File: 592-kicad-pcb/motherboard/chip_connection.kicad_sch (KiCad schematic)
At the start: 12 parts, among them J4 Conn_02x16_Odd_Even, J5 Conn_01x16

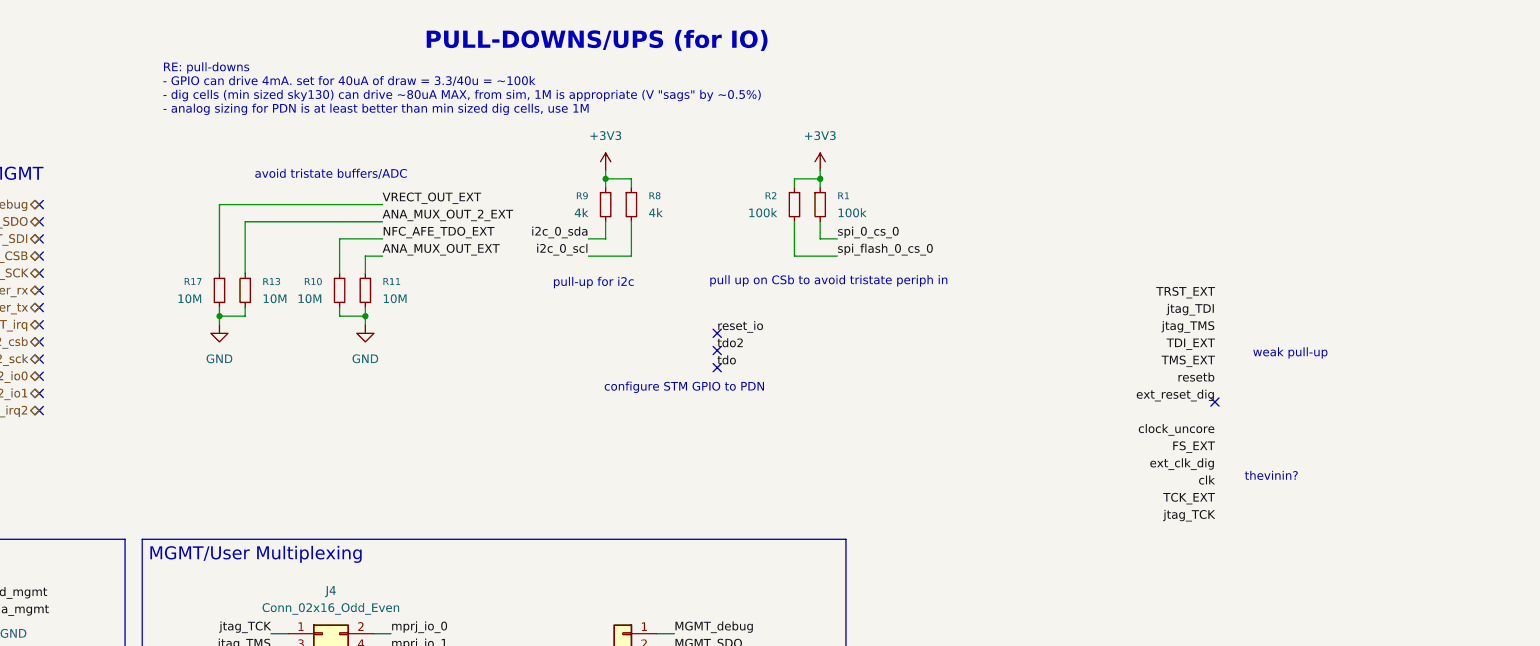
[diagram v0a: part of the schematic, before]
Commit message: update ftdi chip
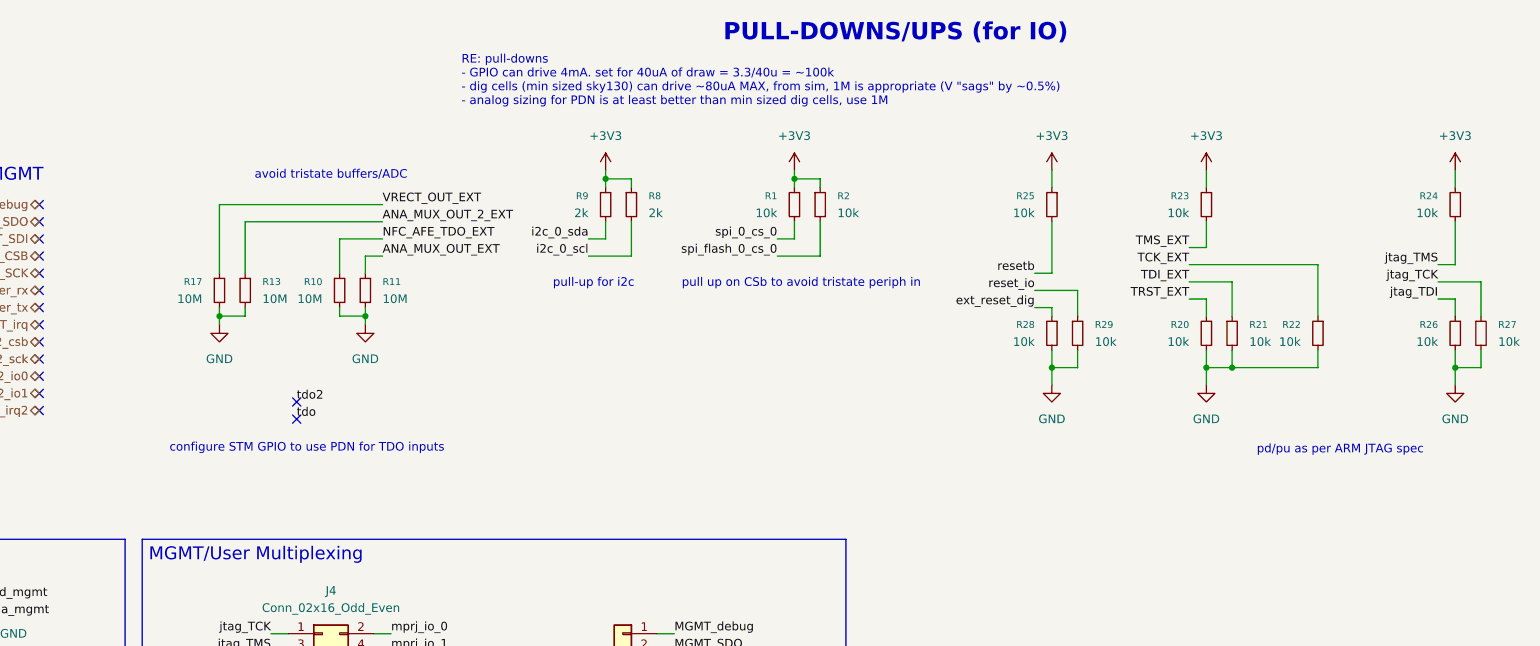
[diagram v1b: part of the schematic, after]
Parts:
- added R20, R21, R22, R23, R24, R25, R26, R27, R28, R29: 10k, symbol Device:R_Small
- R1, R2: value 100k -> 10k
- R8, R9: value 4k -> 2k
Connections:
- net +3V3: now also R23.1, R24.1, R25.1
- net GND: now also R20.2, R21.2, R22.2, R26.2, R27.2, R28.2, R29.2
- net TCK_EXT: now also R22.1
- net TDI_EXT: now also R21.1
- net TMS_EXT: now also R23.2
- net TRST_EXT: now also R20.1
- net ext_reset_dig: now also R28.1
- net jtag_TCK: now also R27.1
- net jtag_TDI: now also R26.1
- net jtag_TMS: now also R24.2
- net reset_io: now also R29.1
- net resetb: now also R25.2
- no-connect marks 65 -> 63
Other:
- note added: "configure STM GPIO to use PDN for TDO inputs"
- note added: "pd/pu as per ARM JTAG spec"
- note removed: "configure STM GPIO to PDN"
- note removed: "thevinin?"
- note removed: "weak pull-up"
- moved on the sheet: R1, R2

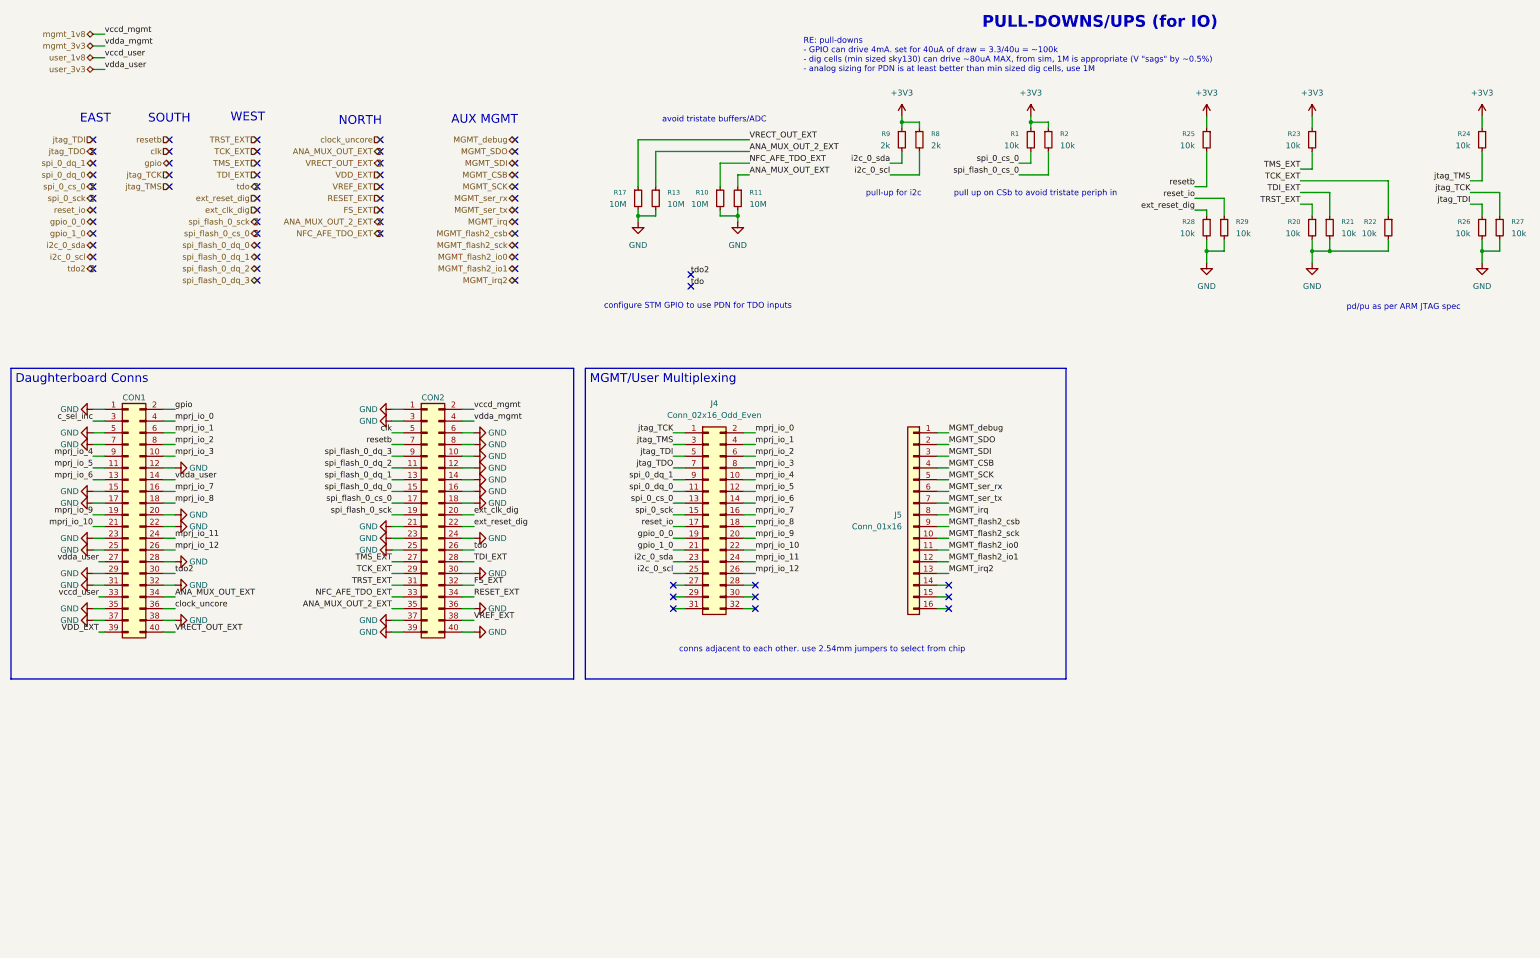
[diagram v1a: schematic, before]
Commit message: combine hierarchy of all sans power
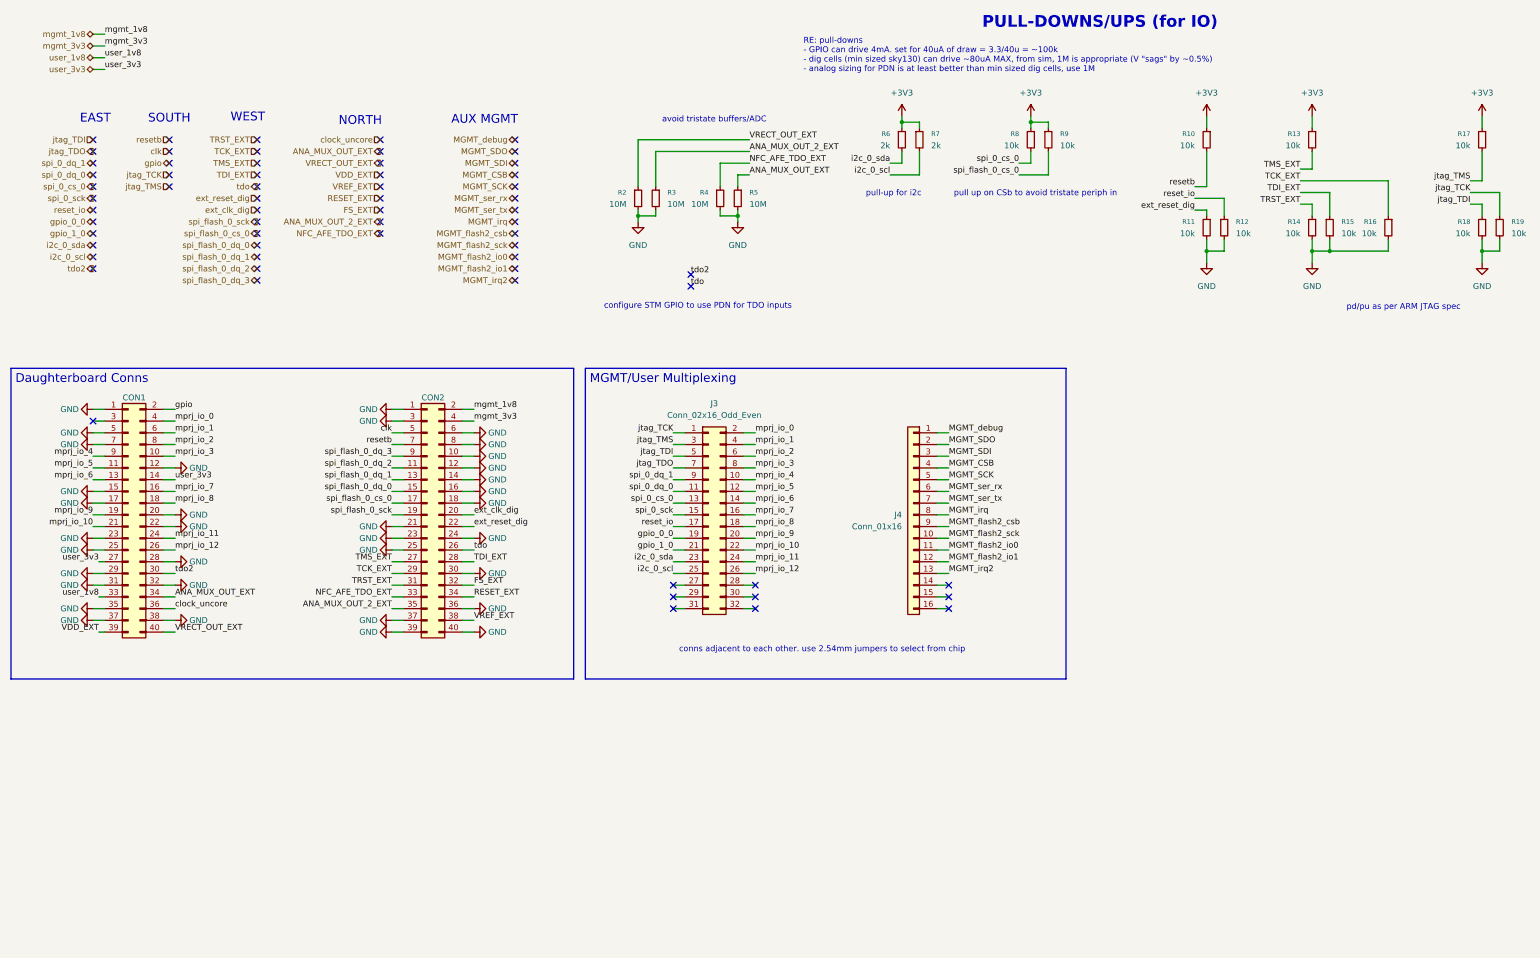
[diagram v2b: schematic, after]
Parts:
- renumbered J4 to J3, J5 to J4, R25 to R10, R28 to R11, R29 to R12, R23 to R13, R20 to R14, R21 to R15, R22 to R16, R24 to R17, R26 to R18, R27 to R19, R17 to R2, R13 to R3, R10 to R4, R11 to R5, R9 to R6, R8 to R7, R1 to R8, R2 to R9
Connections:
- net c_sel_inc: no longer names the net of CON1.3 (Pin_3)
- no-connect marks 63 -> 64

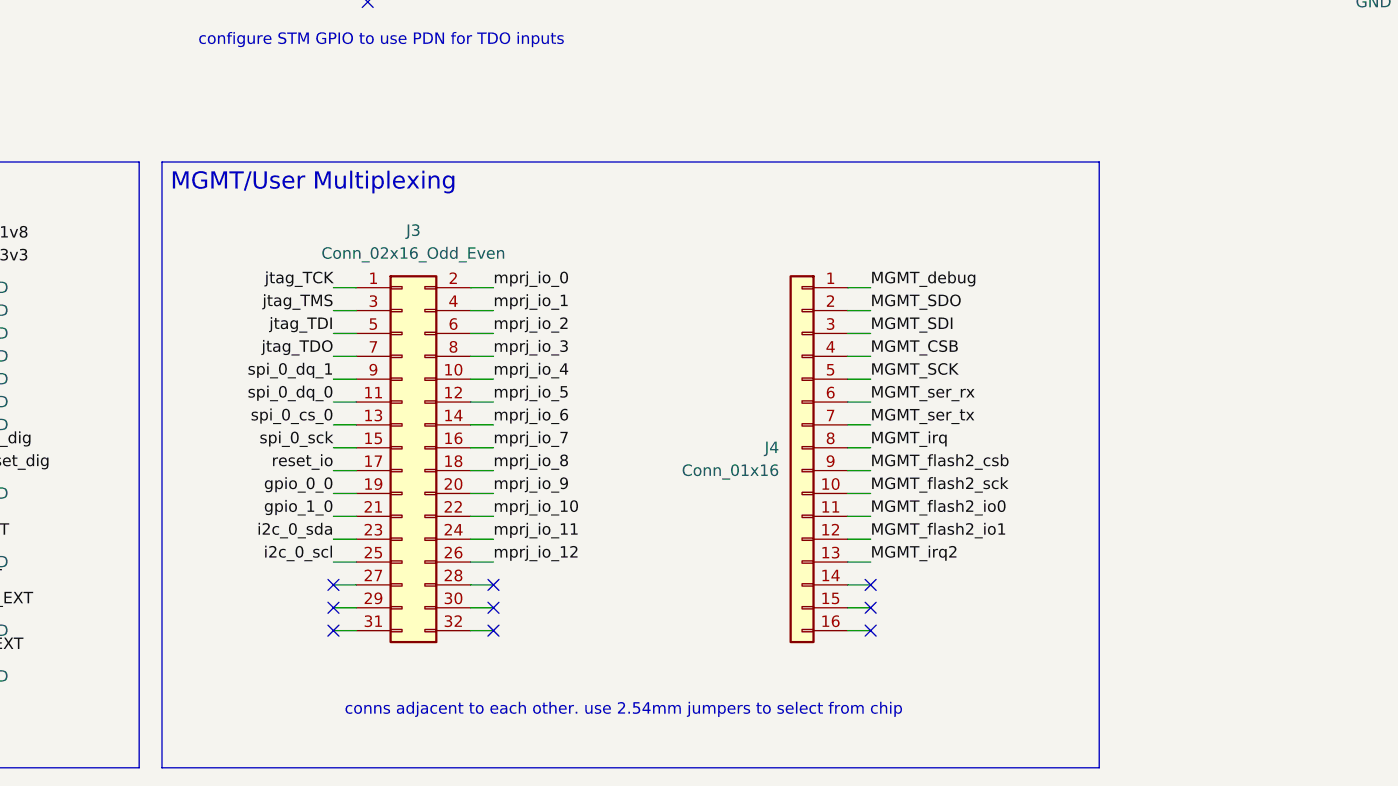
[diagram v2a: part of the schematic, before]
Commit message: add JLC part num for parts, footprints
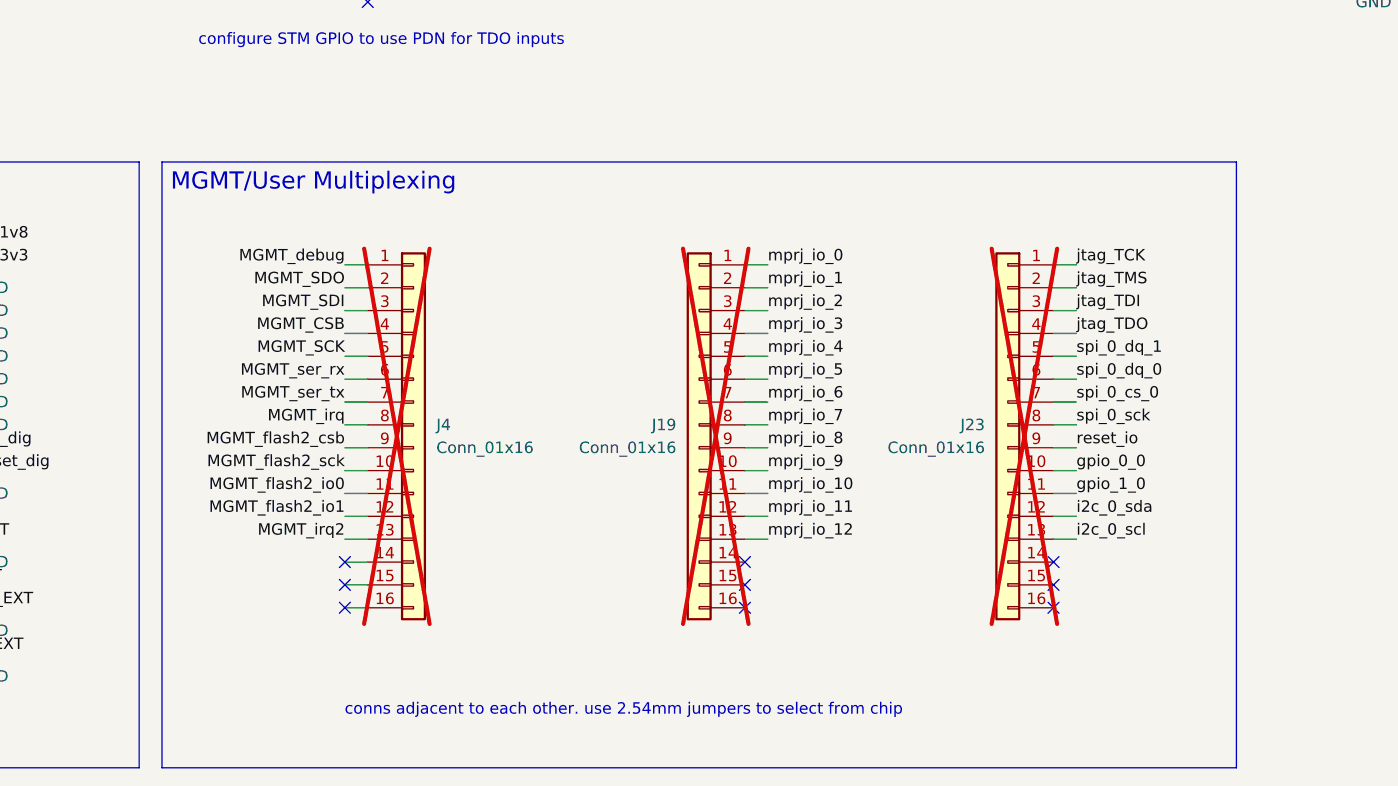
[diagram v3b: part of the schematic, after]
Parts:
- removed J3: Conn_02x16_Odd_Even, symbol Connector_Generic:Conn_02x16_Odd_Even
- added J19, J23: Conn_01x16, Connector_PinHeader_2.54mm:PinHeader_1x16_P2.54mm_Vertical, symbol Connector_Generic:Conn_01x16
- CON1, CON2: footprint TinyTapeout:FH-00148_PinSocket_2x20_P2.54mm -> (none)
- J4: footprint (none) -> Connector_PinHeader_2.54mm:PinHeader_1x16_P2.54mm_Vertical; now not fitted
- R10, R11, R12, R13, R14, R15, R16, R17, R18, R19, R8, R9: footprint (none) -> Resistor_SMD:R_0603_1608Metric; LCSC (none) -> C25804
- R2, R3, R4, R5: footprint (none) -> Resistor_SMD:R_0603_1608Metric; LCSC (none) -> C7250
- R6, R7: footprint (none) -> Resistor_SMD:R_0603_1608Metric; LCSC (none) -> C22975
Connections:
- net gpio_0_0: now also J23.10 (Pin_10)
- net gpio_1_0: now also J23.11 (Pin_11)
- net i2c_0_scl: now also J23.13 (Pin_13)
- net i2c_0_sda: now also J23.12 (Pin_12)
- net jtag_TCK: now also J23.1 (Pin_1)
- net jtag_TDI: now also J23.3 (Pin_3)
- net jtag_TDO: now also J23.4 (Pin_4)
- net jtag_TMS: now also J23.2 (Pin_2)
- net mprj_io_0: now also J19.1 (Pin_1)
- net mprj_io_1: now also J19.2 (Pin_2)
- net mprj_io_10: now also J19.11 (Pin_11)
- net mprj_io_11: now also J19.12 (Pin_12)
- net mprj_io_12: now also J19.13 (Pin_13)
- net mprj_io_2: now also J19.3 (Pin_3)
- net mprj_io_3: now also J19.4 (Pin_4)
- net mprj_io_4: now also J19.5 (Pin_5)
- net mprj_io_5: now also J19.6 (Pin_6)
- net mprj_io_6: now also J19.7 (Pin_7)
- net mprj_io_7: now also J19.8 (Pin_8)
- net mprj_io_8: now also J19.9 (Pin_9)
- net mprj_io_9: now also J19.10 (Pin_10)
- net reset_io: now also J23.9 (Pin_9)
- net spi_0_cs_0: now also J23.7 (Pin_7)
- net spi_0_dq_0: now also J23.6 (Pin_6)
- net spi_0_dq_1: now also J23.5 (Pin_5)
- net spi_0_sck: now also J23.8 (Pin_8)

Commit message: update footprints, final
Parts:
- removed CON1, CON2: ~, symbol Connector_Generic:Conn_02x20_Odd_Even
- added J24, J3: DF40C-40DP-0.4V(51), Connector_Hirose_DF40:Hirose_DF40C(2.0)-40DS-0.4V_2x20_P0.4mm, symbol 592-partslib:DF40C-40DS-0.4V_51_
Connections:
- net ANA_MUX_OUT_2_EXT: now also J24.36
- net ANA_MUX_OUT_EXT: now also J3.33
- net FS_EXT: now also J24.32
- net GND: now also J24.10, J24.12, J24.14, J24.16, J24.18, J24.2, J24.20, J24.21, J24.22, J24.24, J24.26, J24.28, J24.30, J24.39, J24.4, J24.6, J24.8, J3.11, J3.15, J3.17, J3.19, J3.2, J3.21, J3.23, J3.25, J3.27, J3.29, J3.31, J3.32, J3.36, J3.37, J3.38, J3.4, J3.40, J3.6, J3.8
- net NFC_AFE_TDO_EXT: now also J24.40
- net RESET_EXT: now also J24.37
- net TCK_EXT: now also J24.31
- net TDI_EXT: now also J24.27
- net TMS_EXT: now also J24.29
- net TRST_EXT: now also J24.33
- net VDD_EXT: now also J24.38
- net VRECT_OUT_EXT: now also J3.39
- net VREF_EXT: now also J24.35
- net clk: now also J24.5
- net clock_uncore: now also J3.35
- net ext_clk_dig: now also J24.34
- net ext_reset_dig: now also J24.23
- net gpio: now also J3.9
- net mgmt_1v8: now also J24.1
- net mgmt_3v3: now also J24.3
- net mprj_io_0: now also J3.7
- net mprj_io_1: now also J3.5
- net mprj_io_10: now also J3.22
- net mprj_io_11: now also J3.24
- net mprj_io_12: now also J3.26
- net mprj_io_2: now also J3.3
- net mprj_io_3: now also J3.1
- net mprj_io_4: now also J3.10
- net mprj_io_5: now also J3.12
- net mprj_io_6: now also J3.14
- net mprj_io_7: now also J3.16
- net mprj_io_8: now also J3.18
- net mprj_io_9: now also J3.20
- net resetb: now also J24.7
- net spi_flash_0_cs_0: now also J24.17
- net spi_flash_0_dq_0: now also J24.15
- net spi_flash_0_dq_1: now also J24.13
- net spi_flash_0_dq_2: now also J24.11
- net spi_flash_0_dq_3: now also J24.9
- net spi_flash_0_sck: now also J24.19
- net tdo: now also J24.25
- net tdo2: now also J3.30
- net user_1v8: now also J3.34
- net user_3v3: now also J3.13, J3.28
- no-connect marks 64 -> 63
